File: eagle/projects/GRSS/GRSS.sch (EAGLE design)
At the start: 36 parts, among them J1 MOL-SL-2-RA, J10 MOL-SL-2-RA, J11 MOL-SL-2-RA, J2 MOL-SL-2-RA, J3 MOL-SL-2-RA, J4 MOL-SL-2-RA, J5 MOL-SL-2-RA, J6 MOL-SL-2-RA, J7 MOL-SL-2-RA, J8 MOL-SL-2-RA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

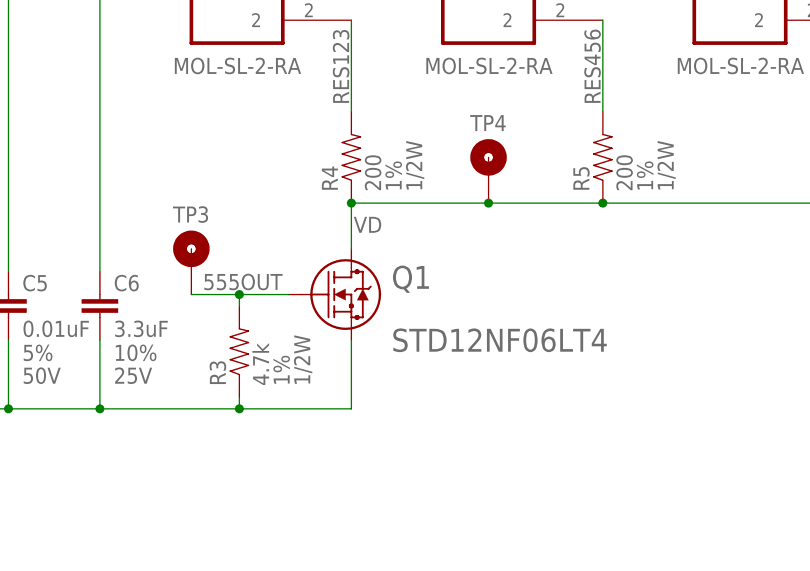
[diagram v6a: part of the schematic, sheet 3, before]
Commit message: Added Zero ohm resistor on FET drain for sys current meas
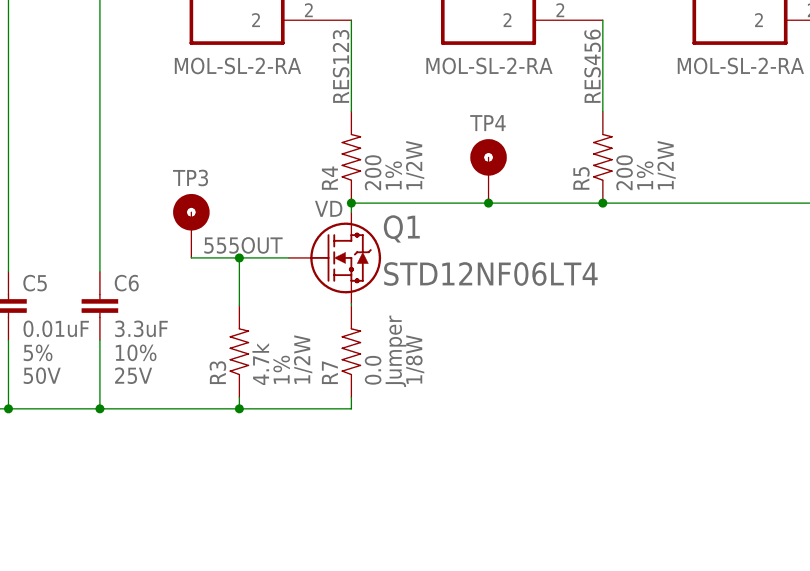
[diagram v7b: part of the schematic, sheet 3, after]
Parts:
- added R7: 0.0, grss:RES_0R0_0805
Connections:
- new net ZEROOHM: Q1.3, R7.2
- net GND: now also R7.1; no longer Q1.3
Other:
- moved on the sheet: Q1, TP3
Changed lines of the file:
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@@
 <part name="R1" library="grss" deviceset="RES" device="_0805" technology="_1K0" value="1k"/>
 <part name="C3" library="grss" deviceset="CAP" device="_0805" technology="_1UF0" value="1uF"/>
+<part name="R7" library="grss" deviceset="RES" device="_0805" technology="_0R0" value="0.0"/>
 </parts>
 <sheets>
@@
 <instance part="U2" gate="A" x="-154.94" y="134.62"/>
 <instance part="U1" gate="A" x="-144.78" y="172.72"/>
-<instance part="Q1" gate="A" x="-27.305" y="104.14"/>
+<instance part="Q1" gate="A" x="-27.305" y="108.204" smashed="yes">
+<attribute name="VALUE" x="-16.891" y="105.156" size="2.54" layer="96" ratio="10" rot="SR0"/>
+<attribute name="NAME" x="-16.891" y="110.363" size="2.54" layer="95" ratio="10" rot="SR0"/>
+</instance>
 <instance part="GND1" gate="1" x="-172.72" y="88.9"/>
 <instance part="J1" gate="G$1" x="-33.02" y="177.8"/>
@@
 <instance part="NC1" gate="G$1" x="-88.9" y="127" rot="R180"/>
 <instance part="TP2" gate="G$1" x="-76.2" y="177.8"/>
-<instance part="TP3" gate="G$1" x="-38.1" y="109.22"/>
+<instance part="TP3" gate="G$1" x="-38.1" y="113.284"/>
 <instance part="TP4" gate="G$1" x="-5.08" y="119.38"/>
 <instance part="H1" gate="G$1" x="-144.78" y="73.66"/>
@@
 <instance part="R1" gate="G$1" x="-68.58" y="139.7" rot="R90"/>
 <instance part="C3" gate="G$1" x="-144.78" y="101.6"/>
+<instance part="R7" gate="G$1" x="-20.32" y="97.79" rot="R90"/>
 </instances>
 <busses>
@@
 <junction x="-172.72" y="91.44"/>
 <pinref part="R3" gate="G$1" pin="1"/>
-<pinref part="Q1" gate="A" pin="3"/>
-<wire x1="-20.32" y1="91.44" x2="-20.32" y2="99.06" width="0.1524" layer="91"/>
 <wire x1="-32.766" y1="91.44" x2="-20.32" y2="91.44" width="0.1524" layer="91"/>
 <wire x1="-32.766" y1="91.44" x2="-32.766" y2="92.71" width="0.1524" layer="91"/>
@@
 <junction x="-68.58" y="91.44"/>
 <junction x="-165.1" y="91.44"/>
+<pinref part="R7" gate="G$1" pin="1"/>
+<wire x1="-20.32" y1="91.44" x2="-20.32" y2="92.71" width="0.1524" layer="91"/>
 </segment>
 </net>
@@
 </segment>
 <segment>
-<wire x1="-27.305" y1="104.14" x2="-32.766" y2="104.14" width="0.1524" layer="91"/>
-<label x="-36.83" y="104.648" size="1.778" layer="95"/>
+<wire x1="-27.305" y1="108.204" x2="-32.766" y2="108.204" width="0.1524" layer="91"/>
+<label x="-36.83" y="108.712" size="1.778" layer="95"/>
 <pinref part="Q1" gate="A" pin="1"/>
 <pinref part="TP3" gate="G$1" pin="TP"/>
 <pinref part="R3" gate="G$1" pin="2"/>
-<wire x1="-32.766" y1="104.14" x2="-38.1" y2="104.14" width="0.1524" layer="91"/>
-<wire x1="-32.766" y1="102.87" x2="-32.766" y2="104.14" width="0.1524" layer="91"/>
-<junction x="-32.766" y="104.14"/>
+<wire x1="-32.766" y1="108.204" x2="-38.1" y2="108.204" width="0.1524" layer="91"/>
+<wire x1="-32.766" y1="102.87" x2="-32.766" y2="108.204" width="0.1524" layer="91"/>
+<junction x="-32.766" y="108.204"/>
 </segment>
 </net>
@@
 <junction x="7.62" y="114.3"/>
 <pinref part="Q1" gate="A" pin="2"/>
-<wire x1="-20.32" y1="109.22" x2="-20.32" y2="114.3" width="0.1524" layer="91"/>
+<wire x1="-20.32" y1="113.284" x2="-20.32" y2="114.3" width="0.1524" layer="91"/>
 <junction x="-20.32" y="114.3"/>
-<label x="-20.066" y="110.998" size="1.778" layer="95"/>
+<label x="-24.384" y="112.776" size="1.778" layer="95"/>
 <pinref part="J10" gate="G$1" pin="2"/>
 <pinref part="TP4" gate="G$1" pin="TP"/>
@@
 </segment>
 </net>
+<net name="ZEROOHM" class="0">
+<segment>
+<pinref part="R7" gate="G$1" pin="2"/>
+<pinref part="Q1" gate="A" pin="3"/>
+<wire x1="-20.32" y1="102.87" x2="-20.32" y2="103.124" width="0.1524" layer="91"/>
+</segment>
+</net>

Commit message: Attempt at LDO / 555 Timer solo Layout
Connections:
- net N$1 renamed NC
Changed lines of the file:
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@@
 </segment>
 </net>
-<net name="N$1" class="0">
+<net name="NC" class="0">
 <segment>
 <pinref part="U2" gate="A" pin="CVOLT"/>
